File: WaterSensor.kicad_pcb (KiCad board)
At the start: 2 copper layers, 304.8 x 304.8 mm, 8 parts, among them J2 Conn_01x03_Pin, Q1 2N3904

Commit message: General cleanup of schematic and PCB
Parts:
- moved H2 162.6 mm to (140.4, 58.4)
- moved H3 162.6 mm to (416.6, 335.3)
- moved H4 162.6 mm to (144.8, 337.2)
- moved J2 162.6 mm to (289.6, 198.1)
- moved Q1 162.6 mm to (281.9, 205.7)
- moved R1 162.6 mm to (289.6, 203.8)
- moved R2 162.6 mm to (288.6, 210.8)
- moved H1 162.6 mm to (420.3, 57.1)

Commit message: Change spiral design to finger design
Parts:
- moved J2 177.8 mm to (396.2, 55.9)
- moved Q1 177.8 mm to (388.6, 63.5)
- moved R1 177.8 mm to (396.2, 61.6)
- moved R2 177.8 mm to (395.3, 68.6)
- moved H4 3.16 mm to (142.2, 335.3)
- moved H2 2.54 mm to (140.4, 61.0)
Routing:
- net PWR_SENSE: track 0.00 -> 36100.5 mm
- net BASE_SENSE: track 35658.6 -> 0.66 mm
- net +5V: track 21.3 -> 25.6 mm
- added copper zone on F.Cu, net BASE_SENSE
- removed copper zone on F.Cu, net PWR_SENSE

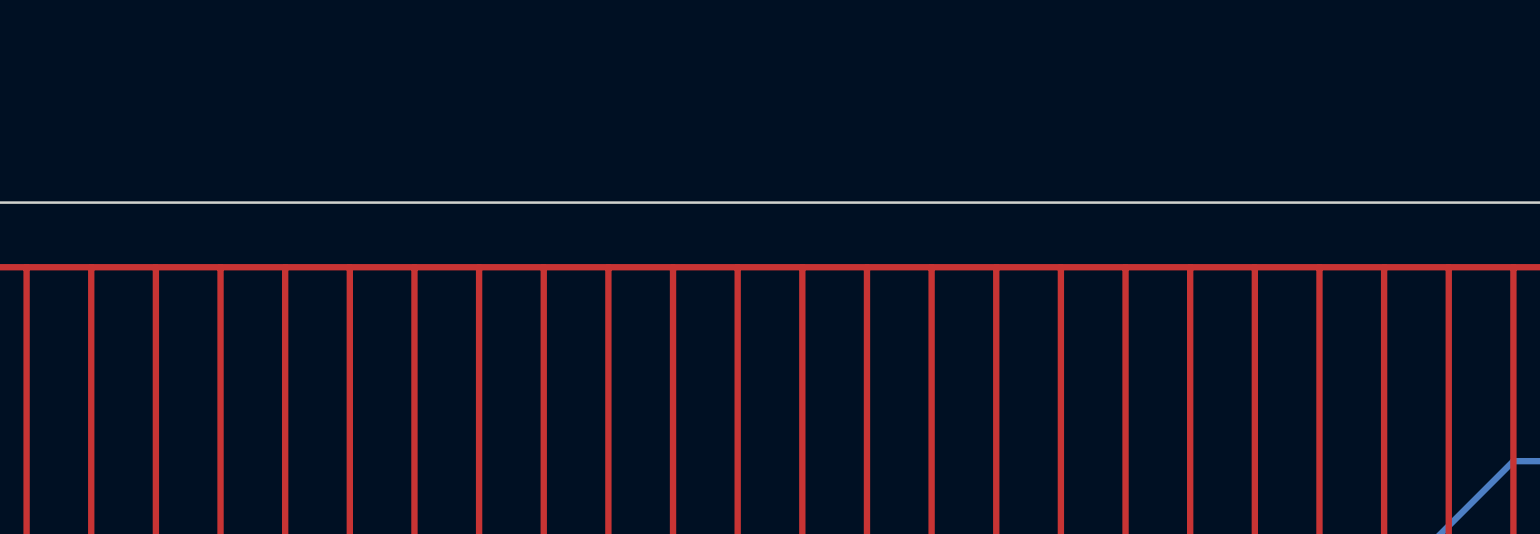
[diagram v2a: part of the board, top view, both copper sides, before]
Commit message: Removed extra back-side ground plane, added silk screen, added front side mask to expose copper
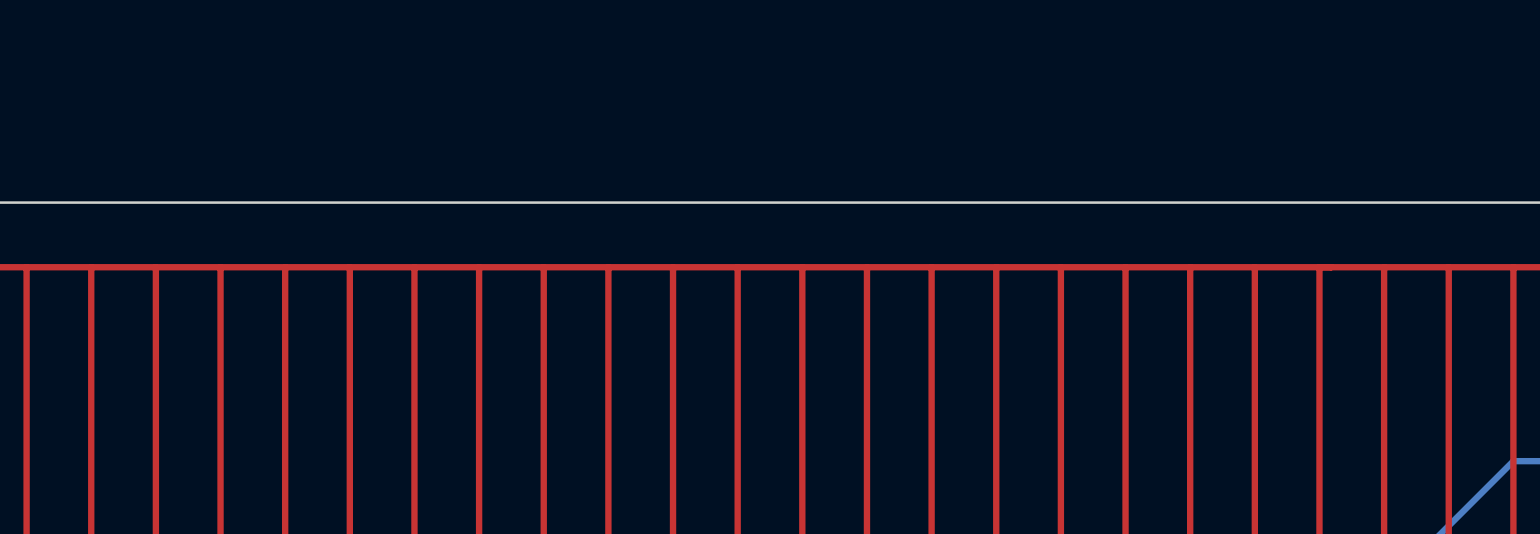
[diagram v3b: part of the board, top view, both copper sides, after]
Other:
- board text added: "+5V"
- board text added: "GND"
- board text added: "SIG"

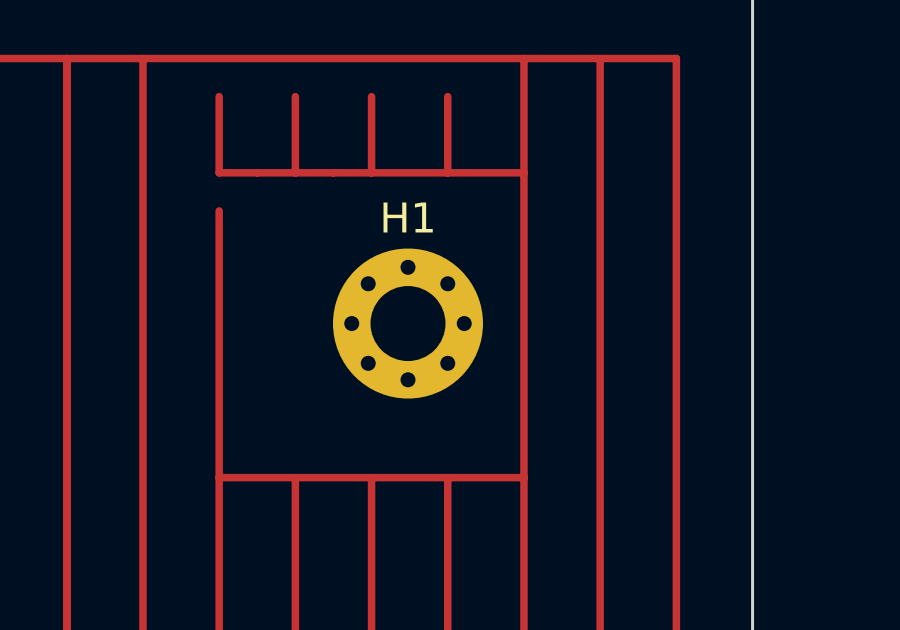
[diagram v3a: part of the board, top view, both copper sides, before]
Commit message: Move H1 text outside of copper region
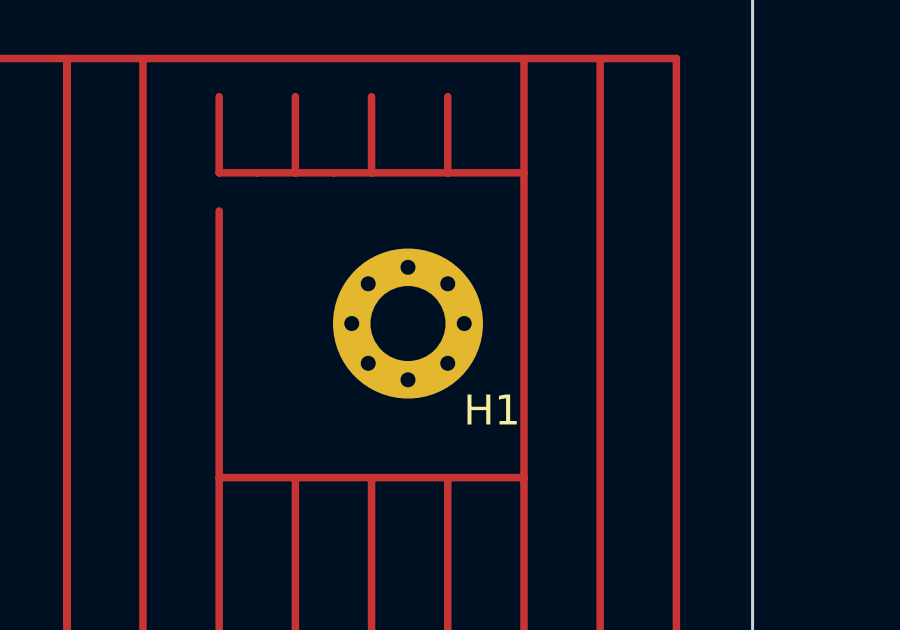
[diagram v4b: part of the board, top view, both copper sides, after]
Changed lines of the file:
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@@
 		(tags "mounting hole 2.5mm")
 		(property "Reference" "H1"
-			(at 0 -3.5 0)
+			(at 2.8 2.9 0)
 			(layer "F.SilkS")
 			(effects
@@
 	)
 	(gr_rect
-		(start 121.92 43.18)
-		(end 439.42 353.06)
-		(stroke
-			(width 0.15)
-			(type solid)
-		)
-		(fill solid)
-		(layer "F.Mask")
-	)
-	(gr_rect
 		(start 127 45.72)
 		(end 431.8 350.52)
@@
 			)
 		)
+	)
+	(zone
+		(net 0)
+		(net_name "")
+		(layer "F.Mask")
+		(hatch edge 0.5)
+		(connect_pads
+			(clearance 0)
+		)
+		(min_thickness 0.25)
+		(filled_areas_thickness no)
+		(fill yes
+			(thermal_gap 0.5)
+			(thermal_bridge_width 0.5)
+		)
+		(polygon
+			(pts
+				(xy 436.88 41.91) (xy 123.19 40.64) (xy 121.92 355.6) (xy 439.42 355.6)
+			)
+		)
